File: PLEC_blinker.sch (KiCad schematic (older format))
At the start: 4 parts, among them Q1 KSC2073H2TU

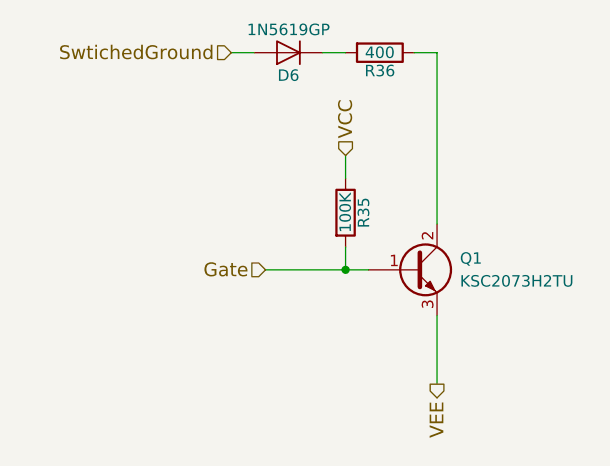
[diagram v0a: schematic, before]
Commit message: Almost done with layout; need to rearrange uC pins
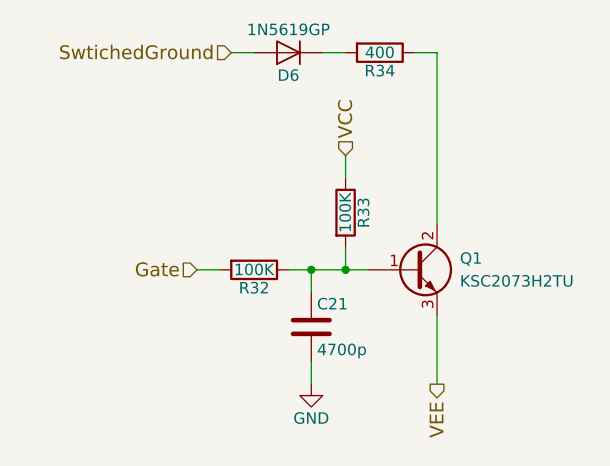
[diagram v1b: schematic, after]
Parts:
- added C21: 4700p, PLEC:THTt_100Px150Lx100Wx183H_4700p, symbol C
- added R32: 100K, Resistors_THT:R_Axial_DIN0204_L3.6mm_D1.6mm_P5.08mm_Horizontal, symbol R
- renumbered R35 to R33, R36 to R34
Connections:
- net Gate: now also R32.2; no longer Q1.1 (B), R33.2
- new net: C21.1, Q1.1 (B), R32.1, R33.2
- new net GND: C21.2
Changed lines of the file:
@@
 $EndDescr
 $Comp
-L R R35
+L R R33
 U 1 1 5A752013
 P 4500 3700
-F 0 "R35" V 4580 3700 50  0000 C CNN
+F 0 "R33" V 4580 3700 50  0000 C CNN
 F 1 "100K" V 4500 3700 50  0000 C CNN
 F 2 "Resistors_THT:R_Axial_DIN0204_L3.6mm_D1.6mm_P5.08mm_Horizontal" V 4430 3700 50  0001 C CNN
@@
 $EndComp
 $Comp
-L R R36
+L R R34
 U 1 1 5A752191
 P 4650 3000
-F 0 "R36" V 4730 3000 50  0000 C CNN
+F 0 "R34" V 4730 3000 50  0000 C CNN
 F 1 "400" V 4650 3000 50  0000 C CNN
 F 2 "Resistors_THT:R_Axial_DIN0207_L6.3mm_D2.5mm_P10.16mm_Horizontal" V 4580 3000 50  0001 C CNN
@@
 Text HLabel 4000 3000 0    60   Input ~ 0
 SwtichedGround
-Wire Wire Line
-	4150 3950 4600 3950
 Text HLabel 4900 4450 3    60   Output ~ 0
 VEE
@@
 Wire Wire Line
 	4500 3550 4500 3450
-Text HLabel 4150 3950 0    60   Input ~ 0
+Text HLabel 3850 3950 0    60   Input ~ 0
 Gate
 Wire Wire Line
@@
 Wire Wire Line
 	4100 3000 4000 3000
+$Comp
+L R R32
+U 1 1 5A7C8ABB
+P 4100 3950
+F 0 "R32" V 4180 3950 50  0000 C CNN
+F 1 "100K" V 4100 3950 50  0000 C CNN
+F 2 "Resistors_THT:R_Axial_DIN0204_L3.6mm_D1.6mm_P5.08mm_Horizontal" V 4030 3950 50  0001 C CNN
+F 3 "" H 4100 3950 50  0001 C CNN
+	1    4100 3950
+	0    1    1    0
+$EndComp
+$Comp
+L C C21
+U 1 1 5A7C8DDF
+P 4350 4200
+F 0 "C21" H 4375 4300 50  0000 L CNN
+F 1 "4700p" H 4375 4100 50  0000 L CNN
+F 2 "PLEC:THTt_100Px150Lx100Wx183H_4700p" H 4388 4050 50  0001 C CNN
+F 3 "" H 4350 4200 50  0001 C CNN
+	1    4350 4200
+	1    0    0    -1
+$EndComp
+$Comp
+L GND #PWR011
+U 1 1 5A7C8E6E
+P 4350 4450
+F 0 "#PWR011" H 4350 4200 50  0001 C CNN
+F 1 "GND" H 4350 4300 50  0000 C CNN
+F 2 "" H 4350 4450 50  0001 C CNN
+F 3 "" H 4350 4450 50  0001 C CNN
+	1    4350 4450
+	1    0    0    -1
+$EndComp
+Wire Wire Line
+	4350 4450 4350 4350
+Wire Wire Line
+	4350 4050 4350 3950
+Connection ~ 4350 3950
+Wire Wire Line
+	4250 3950 4600 3950
+Wire Wire Line
+	3950 3950 3850 3950
 $EndSCHEMATC

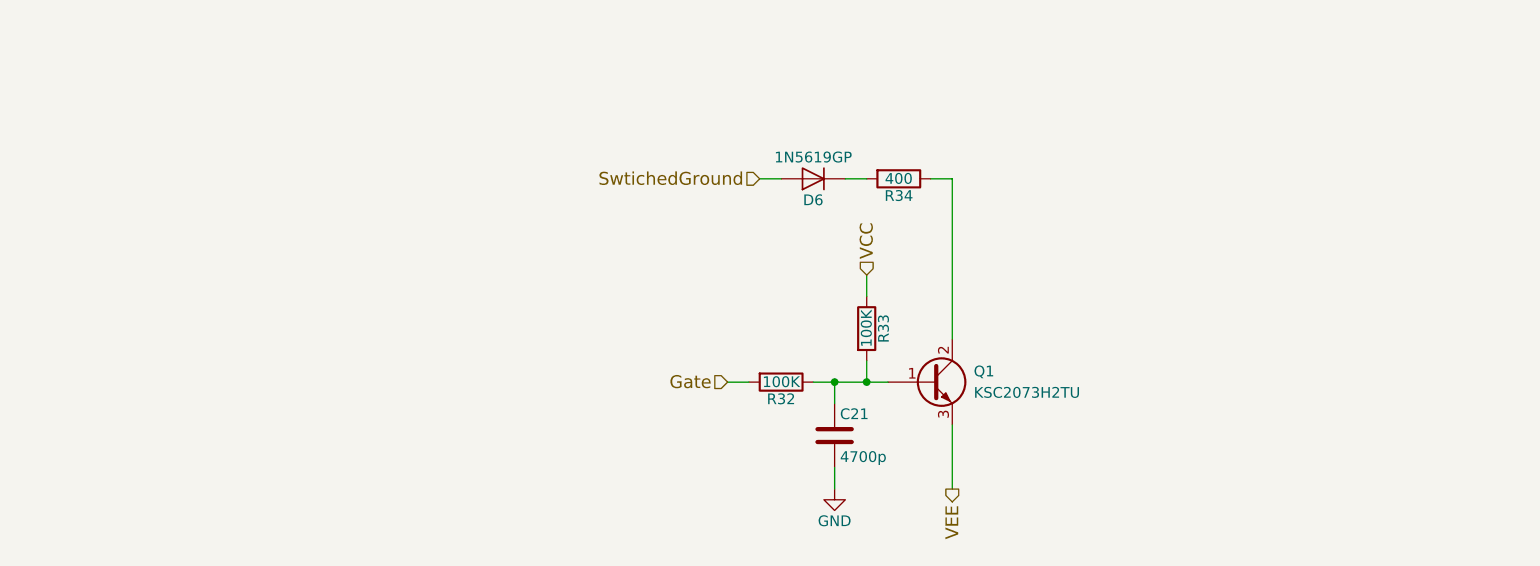
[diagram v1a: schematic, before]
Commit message: Replaced solid state relays with NPN Darlingtons
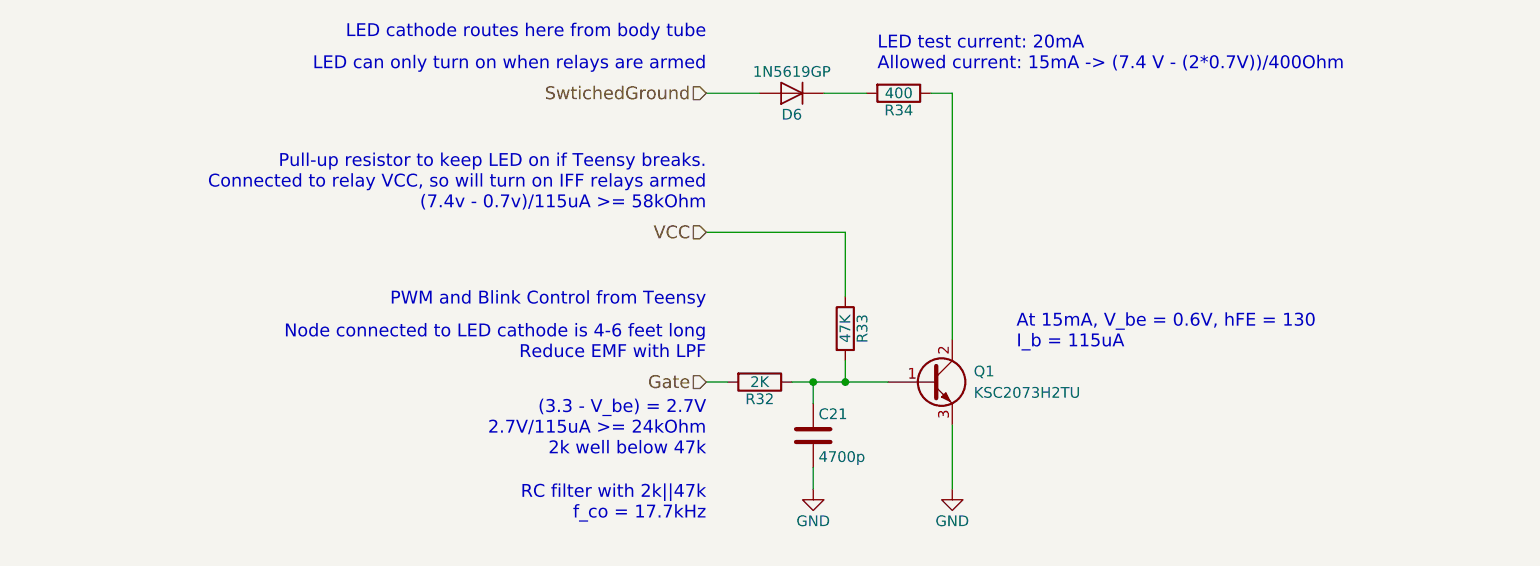
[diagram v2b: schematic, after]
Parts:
- D6: footprint Diodes_THT:D_DO-15_P10.16mm_Horizontal -> Diodes_THT:D_DO-41_SOD81_P2.54mm_Vertical_KathodeUp
- R32: value 100K -> 2K
- R33: value 100K -> 47K
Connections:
- net VEE is gone; now on net GND: Q1.3 (E)
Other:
- note added: "(3.3 - V_be) = 2.7V\n2.7V/115uA >= 24kOhm\n2k well below 47k"
- note added: "At 15mA, V_be = 0.6V, hFE = 130\nI_b = 115uA"
- note added: "LED can only turn on when relays are armed"
- note added: "LED cathode routes here from body tube"
- note added: "LED test current: 20mA\nAllowed current: 15mA -> (7.4 V - (2*0.7V))/400Ohm"
- note added: "Node connected to LED cathode is 4-6 feet long\nReduce EMF with LPF\n"
- note added: "PWM and Blink Control from Teensy"
- note added: "Pull-up resistor to keep LED on if Teensy breaks.\nConnected to relay VCC, so will turn on IFF relays armed\n(7.4v - 0.7v)/115uA >= 58kOhm"
- note added: "RC filter with 2k||47k\nf_co = 17.7kHz"
- moved on the sheet: C21, D6, R32, R33, R34
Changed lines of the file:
@@
 EESchema Schematic File Version 2
+LIBS:PLEC-rescue
 LIBS:power
 LIBS:device
@@
 LIBS:PLEC
 LIBS:cap_470u
+LIBS:BDW42G
 LIBS:PLEC-cache
 EELAYER 25 0
@@
 $Descr A4 11693 8268
 encoding utf-8
-Sheet 6 9
+Sheet 5 9
 Title ""
 Date ""
@@
 L R R33
 U 1 1 5A752013
-P 4500 3700
-F 0 "R33" V 4580 3700 50  0000 C CNN
-F 1 "100K" V 4500 3700 50  0000 C CNN
-F 2 "Resistors_THT:R_Axial_DIN0204_L3.6mm_D1.6mm_P5.08mm_Horizontal" V 4430 3700 50  0001 C CNN
-F 3 "" H 4500 3700 50  0001 C CNN
-	1    4500 3700
+P 4400 3700
+F 0 "R33" V 4480 3700 50  0000 C CNN
+F 1 "47K" V 4400 3700 50  0000 C CNN
+F 2 "Resistors_THT:R_Axial_DIN0204_L3.6mm_D1.6mm_P5.08mm_Horizontal" V 4330 3700 50  0001 C CNN
+F 3 "" H 4400 3700 50  0001 C CNN
+	1    4400 3700
 	1    0    0    -1
 $EndComp
@@
 L D D6
 U 1 1 5A752052
-P 4250 3000
-F 0 "D6" H 4250 3100 50  0000 C CNN
-F 1 "1N5619GP" H 4250 2900 50  0000 C CNN
-F 2 "Diodes_THT:D_DO-15_P10.16mm_Horizontal" H 4250 3000 50  0001 C CNN
-F 3 "" H 4250 3000 50  0001 C CNN
-	1    4250 3000
+P 4150 2600
+F 0 "D6" H 4150 2700 50  0000 C CNN
+F 1 "1N5619GP" H 4150 2500 50  0000 C CNN
+F 2 "Diodes_THT:D_DO-41_SOD81_P2.54mm_Vertical_KathodeUp" H 4150 2600 50  0001 C CNN
+F 3 "" H 4150 2600 50  0001 C CNN
+	1    4150 2600
 	-1   0    0    1
 $EndComp
@@
 L R R34
 U 1 1 5A752191
-P 4650 3000
-F 0 "R34" V 4730 3000 50  0000 C CNN
-F 1 "400" V 4650 3000 50  0000 C CNN
-F 2 "Resistors_THT:R_Axial_DIN0207_L6.3mm_D2.5mm_P10.16mm_Horizontal" V 4580 3000 50  0001 C CNN
-F 3 "" H 4650 3000 50  0001 C CNN
-	1    4650 3000
+P 4650 2600
+F 0 "R34" V 4730 2600 50  0000 C CNN
+F 1 "400" V 4650 2600 50  0000 C CNN
+F 2 "Resistors_THT:R_Axial_DIN0207_L6.3mm_D2.5mm_P10.16mm_Horizontal" V 4580 2600 50  0001 C CNN
+F 3 "" H 4650 2600 50  0001 C CNN
+	1    4650 2600
 	0    1    1    0
 $EndComp
-Text HLabel 4000 3000 0    60   Input ~ 0
+Text HLabel 3750 2600 0    60   Input ~ 0
 SwtichedGround
-Text HLabel 4900 4450 3    60   Output ~ 0
-VEE
 Wire Wire Line
-	4500 3950 4500 3850
-Connection ~ 4500 3950
-Text HLabel 4500 3450 1    60   Input ~ 0
-VCC
-Wire Wire Line
-	4500 3550 4500 3450
-Text HLabel 3850 3950 0    60   Input ~ 0
+	4400 3950 4400 3850
+Connection ~ 4400 3950
+Text HLabel 3750 3950 0    60   Input ~ 0
 Gate
 Wire Wire Line
 	4900 4450 4900 4150
 Wire Wire Line
-	4900 3000 4900 3750
+	4900 2600 4900 3750
 Wire Wire Line
-	4400 3000 4500 3000
+	4300 2600 4500 2600
 Wire Wire Line
-	4900 3000 4800 3000
+	4900 2600 4800 2600
 Wire Wire Line
-	4100 3000 4000 3000
+	4000 2600 3750 2600
 $Comp
 L R R32
 U 1 1 5A7C8ABB
-P 4100 3950
-F 0 "R32" V 4180 3950 50  0000 C CNN
-F 1 "100K" V 4100 3950 50  0000 C CNN
-F 2 "Resistors_THT:R_Axial_DIN0204_L3.6mm_D1.6mm_P5.08mm_Horizontal" V 4030 3950 50  0001 C CNN
-F 3 "" H 4100 3950 50  0001 C CNN
-	1    4100 3950
+P 4000 3950
+F 0 "R32" V 4080 3950 50  0000 C CNN
+F 1 "2K" V 4000 3950 50  0000 C CNN
+F 2 "Resistors_THT:R_Axial_DIN0204_L3.6mm_D1.6mm_P5.08mm_Horizontal" V 3930 3950 50  0001 C CNN
+F 3 "" H 4000 3950 50  0001 C CNN
+	1    4000 3950
 	0    1    1    0
 $EndComp
@@
 L C C21
 U 1 1 5A7C8DDF
-P 4350 4200
-F 0 "C21" H 4375 4300 50  0000 L CNN
-F 1 "4700p" H 4375 4100 50  0000 L CNN
-F 2 "PLEC:THTt_100Px150Lx100Wx183H_4700p" H 4388 4050 50  0001 C CNN
-F 3 "" H 4350 4200 50  0001 C CNN
-	1    4350 4200
+P 4250 4200
+F 0 "C21" H 4275 4300 50  0000 L CNN
+F 1 "4700p" H 4275 4100 50  0000 L CNN
+F 2 "PLEC:THTt_100Px150Lx100Wx183H_4700p" H 4288 4050 50  0001 C CNN
+F 3 "" H 4250 4200 50  0001 C CNN
+	1    4250 4200
 	1    0    0    -1
 $EndComp
 $Comp
-L GND #PWR011
+L GND #PWR026
 U 1 1 5A7C8E6E
-P 4350 4450
-F 0 "#PWR011" H 4350 4200 50  0001 C CNN
-F 1 "GND" H 4350 4300 50  0000 C CNN
-F 2 "" H 4350 4450 50  0001 C CNN
-F 3 "" H 4350 4450 50  0001 C CNN
-	1    4350 4450
+P 4250 4450
+F 0 "#PWR026" H 4250 4200 50  0001 C CNN
+F 1 "GND" H 4250 4300 50  0000 C CNN
+F 2 "" H 4250 4450 50  0001 C CNN
+F 3 "" H 4250 4450 50  0001 C CNN
+	1    4250 4450
 	1    0    0    -1
 $EndComp
 Wire Wire Line
-	4350 4450 4350 4350
+	4250 4450 4250 4350
 Wire Wire Line
-	4350 4050 4350 3950
-Connection ~ 4350 3950
+	4250 4050 4250 3950
+Connection ~ 4250 3950
 Wire Wire Line
-	4250 3950 4600 3950
+	4150 3950 4600 3950
 Wire Wire Line
-	3950 3950 3850 3950
+	3850 3950 3750 3950
+$Comp
+L GND #PWR027
+U 1 1 5A850FBF
+P 4900 4450
+F 0 "#PWR027" H 4900 4200 50  0001 C CNN
+F 1 "GND" H 4900 4300 50  0000 C CNN
+F 2 "" H 4900 4450 50  0001 C CNN
+F 3 "" H 4900 4450 50  0001 C CNN
+	1    4900 4450
+	1    0    0    -1
+$EndComp
+Text Notes 3750 2500 2    60   ~ 0
+LED can only turn on when relays are armed
+Text Notes 3750 3600 2    60   ~ 0
+PWM and Blink Control from Teensy
+Text Notes 3750 3850 2    60   ~ 0
+Node connected to LED cathode is 4-6 feet long\nReduce EMF with LPF\n
+Text Notes 3750 2350 2    60   ~ 0
+LED cathode routes here from body tube
+Wire Wire Line
+	4400 3550 4400 3250
+Wire Wire Line
+	4400 3250 3750 3250
+Text HLabel 3750 3250 0    60   Input ~ 0
+VCC
+Text Notes 3750 3150 2    60   ~ 0
+Pull-up resistor to keep LED on if Teensy breaks.\nConnected to relay VCC, so will turn on IFF relays armed\n(7.4v - 0.7v)/115uA >= 58kOhm
+Text Notes 4550 2500 0    60   ~ 0
+LED test current: 20mA\nAllowed current: 15mA -> (7.4 V - (2*0.7V))/400Ohm
+Text Notes 5200 3800 0    60   ~ 0
+At 15mA, V_be = 0.6V, hFE = 130\nI_b = 115uA
+Text Notes 3750 4300 2    60   ~ 0
+(3.3 - V_be) = 2.7V\n2.7V/115uA >= 24kOhm\n2k well below 47k
+Text Notes 3750 4600 2    60   ~ 0
+RC filter with 2k||47k\nf_co = 17.7kHz
 $EndSCHEMATC
